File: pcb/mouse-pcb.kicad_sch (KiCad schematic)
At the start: 19 parts, among them J1 TYPE-C-31-M-12, SW1 D2FC-F-7N20M, SW2 D2FC-F-7N20M, SW3 D2FC-F-7N20M, U1 PAW3395-T6QU, U2 NRF52840-QIAA-R7

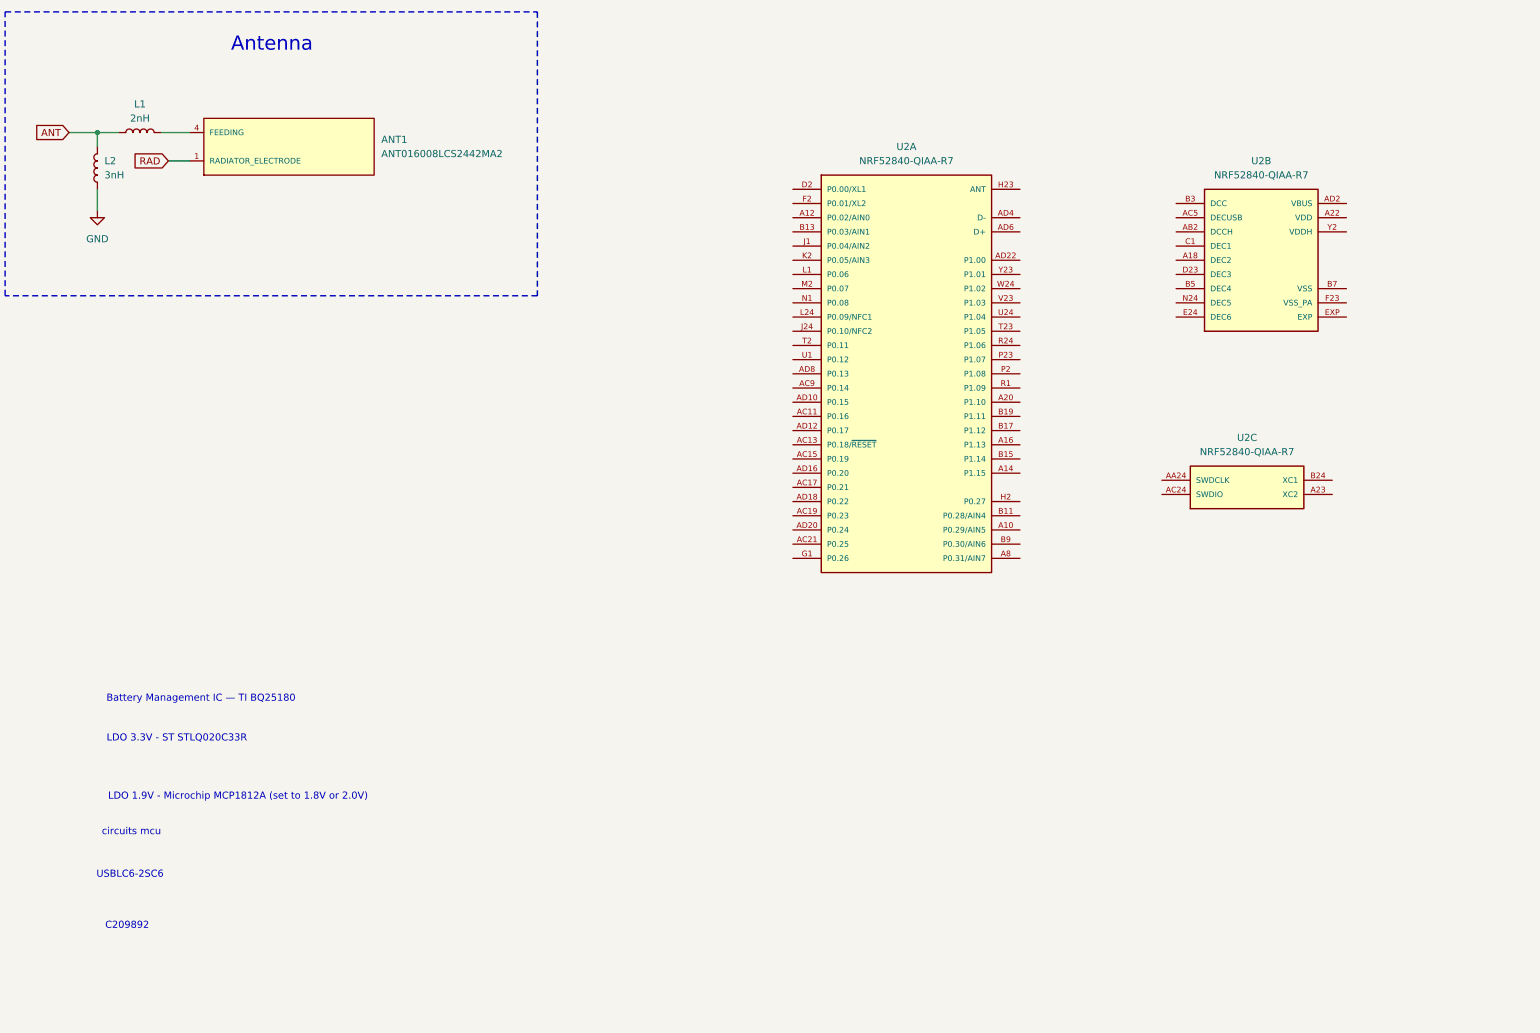
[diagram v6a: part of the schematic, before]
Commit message: ci: ci implemented for kicad
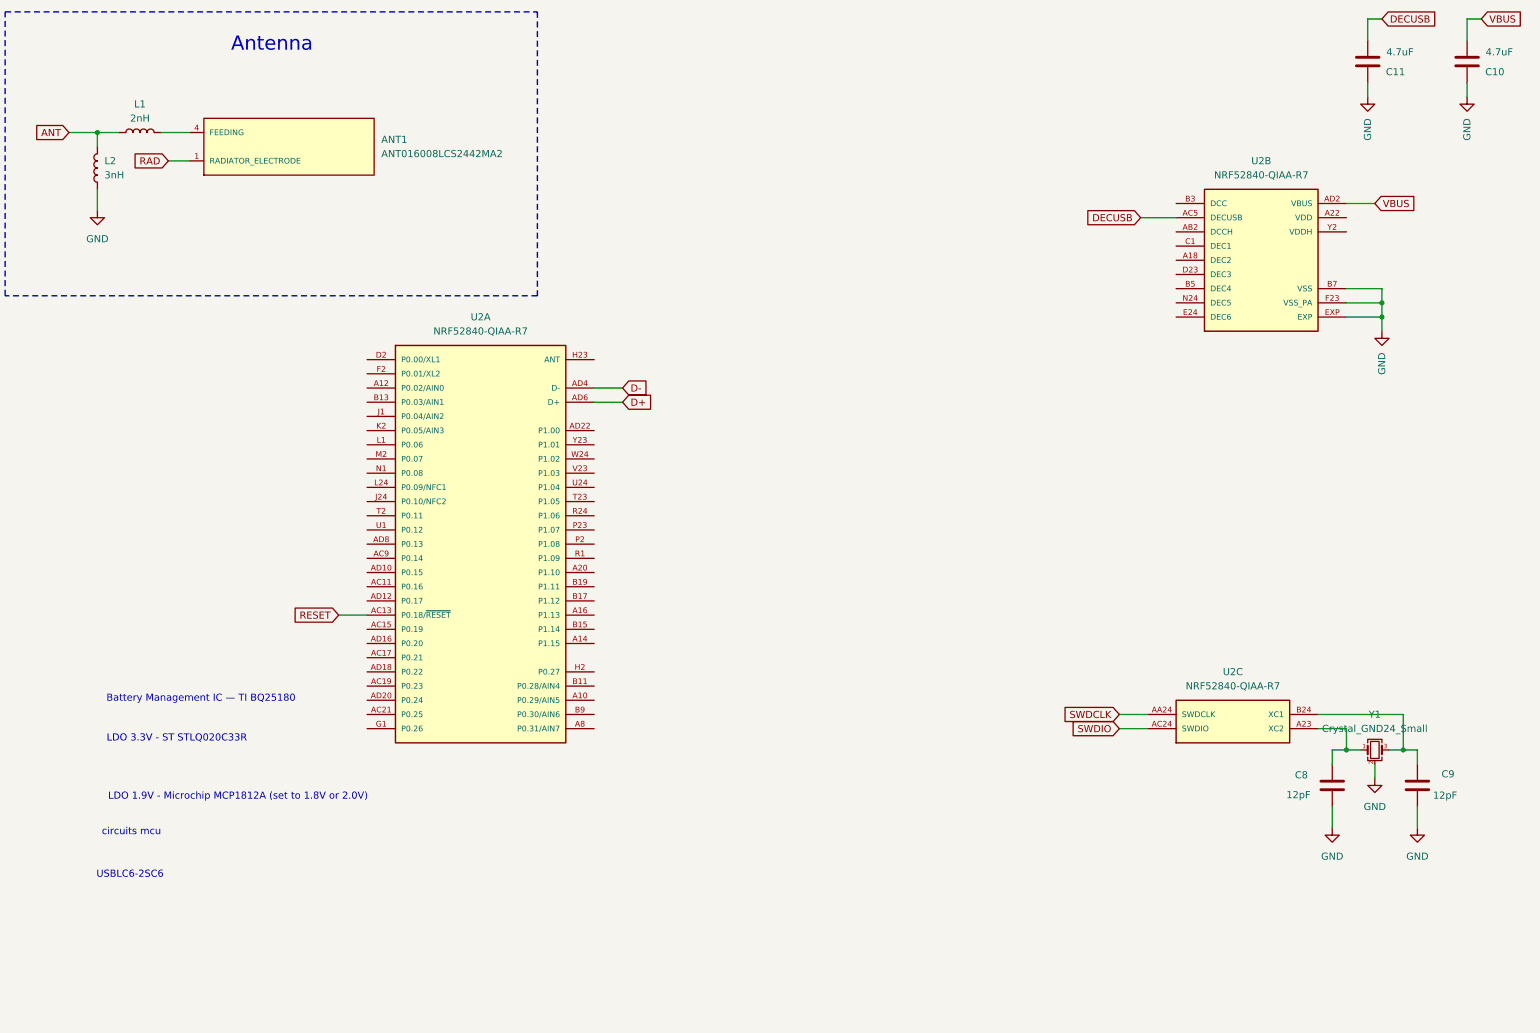
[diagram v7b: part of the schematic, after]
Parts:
- added C10, C11: 4.7uF, Capacitor_SMD:C_0402_1005Metric, symbol Device:C
- added C8, C9: 12pF, Capacitor_SMD:C_0402_1005Metric, symbol Device:C
- added Y1: Crystal_GND24_Small, Crystal:Crystal_SMD_WE_IQXC-42-4Pin_2.0x1.6mm, symbol Device:Crystal_GND24_Small
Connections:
- net GND: now also U2.B7 (VSS), U2.EXP, U2.F23 (VSS_PA), C10.1, C11.1, C8.2, C9.2, Y1.2 (G), Y1.4 (G)
- net VBUS: now also U2.AD2 (VBUS), C10.2
- net DECUSB: now reaches U2.AC5 (DECUSB)
- net DECUSB: now also C11.2
- net at U2.A23 (XC2): now also C8.1, Y1.1
- net SWDCLK: now reaches U2.AA24 (SWDCLK)
- net SWDIO: now reaches U2.AC24 (SWDIO)
- net at U2.B24 (XC1): now also C9.1, Y1.3
- net RESET: now reaches U2.AC13 (P0.18/~{RESET})
- net D-: now reaches U2.AD4 (D-)
- net D+: now reaches U2.AD6 (D+)
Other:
- note removed: "C209892"
- moved on the sheet: U2A, U2C

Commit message: feat: all micro circuits added
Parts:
- added C12, C17: 4.7uF, Capacitor_SMD:C_0402_1005Metric, symbol Device:C
- added C13, C18: 1.0uF, Capacitor_SMD:C_0402_1005Metric, symbol Device:C
- added C14, C15, C16, C21: 100nF, Capacitor_SMD:C_0402_1005Metric, symbol Device:C
- added C19: 47nF, Capacitor_SMD:C_0402_1005Metric, symbol Device:C
- added C20: C, Capacitor_SMD:C_0402_1005Metric, symbol Device:C
- added C22: 100pF, Capacitor_SMD:C_0402_1005Metric, symbol Device:C
- added C23: 0.8pF, Capacitor_SMD:C_0402_1005Metric, symbol Device:C
- added C24, C25: 0.5pF, Capacitor_SMD:C_0402_1005Metric, symbol Device:C
- added C26, C27: 12pF, Capacitor_SMD:C_0402_1005Metric, symbol Device:C
- added L3, L4: 10uH, Inductor_SMD:L_0402_1005Metric, symbol Device:L
- added L5: 15nH, Inductor_SMD:L_0402_1005Metric, symbol Device:L
- added L6: 4.7nH, Inductor_SMD:L_0201_0603Metric, symbol Device:L
- added Y2: 32.768kHz, Crystal:Crystal_SMD_3215-2Pin_3.2x1.5mm, symbol Device:Crystal_Small
- Y1: value Crystal_GND24_Small -> 32MHz
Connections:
- net ANT: now also C24.2, C25.2, L6.2
- net GND: now also C12.1, C13.1, C14.1, C15.1, C16.1, C17.1, C18.1, C19.1, C20.1, C21.1, C22.1, C23.1, C24.1, C25.1, C26.1, C27.2
- net MISO: now also U2.U24 (P1.04)
- net MOSI: now also U2.R24 (P1.06)
- net MOTION: now also U2.J24 (P0.10/NFC2)
- net NCS: now also U2.R1 (P1.09)
- net NRESET: now also U2.W24 (P1.02)
- net VDD: now also C12.2, C13.2, C14.2, C15.2, C16.2, L3.1
- net DCCH: now reaches U2.AB2 (DCCH)
- net DCCH: now also L3.2
- net DCC: now reaches U2.B3 (DCC)
- net DCC: now also L4.2
- net DEC4: now reaches U2.B5 (DEC4)
- net DEC4: now also U2.E24 (DEC6), C18.2, C19.2, C20.2, L5.1
- net DEC1: now reaches U2.C1 (DEC1)
- net DEC1: now also C21.2
- net DEC3: now reaches U2.D23 (DEC3)
- net DEC3: now also C22.2
- net VDDH: now reaches U2.Y2 (VDDH)
- net VDDH: now also C17.2
- net at U2.D2 (P0.00/XL1): now also C26.2, Y2.1
- net at U2.F2 (P0.01/XL2): now also C27.1, Y2.2
- net ANT_nrf: now reaches U2.H23 (ANT)
- net ANT_nrf: now also C23.2, L6.1
- new net: L4.1, L5.2
- no-connect marks 0 -> 41
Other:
- note added: "MCU"
- note added: "Power"
- note added: "Programmer"
- moved on the sheet: C1, C10, C11, C2, C3, C4, C5, C6, C7, C8, C9, J1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
